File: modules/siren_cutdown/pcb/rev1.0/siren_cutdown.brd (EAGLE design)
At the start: 23.8 x 33.5 mm, 18 parts, among them IC2 PICAXE-08M2

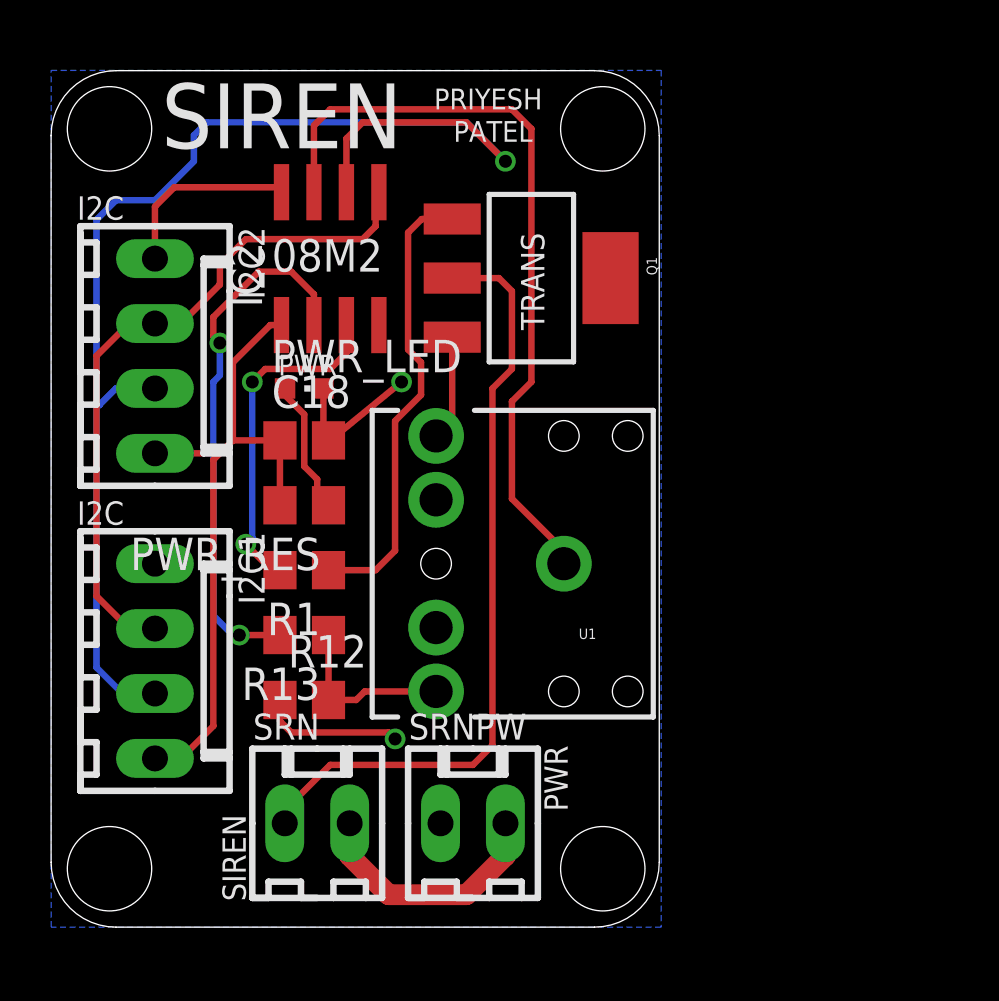
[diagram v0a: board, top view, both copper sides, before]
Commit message: added cutdown to siren
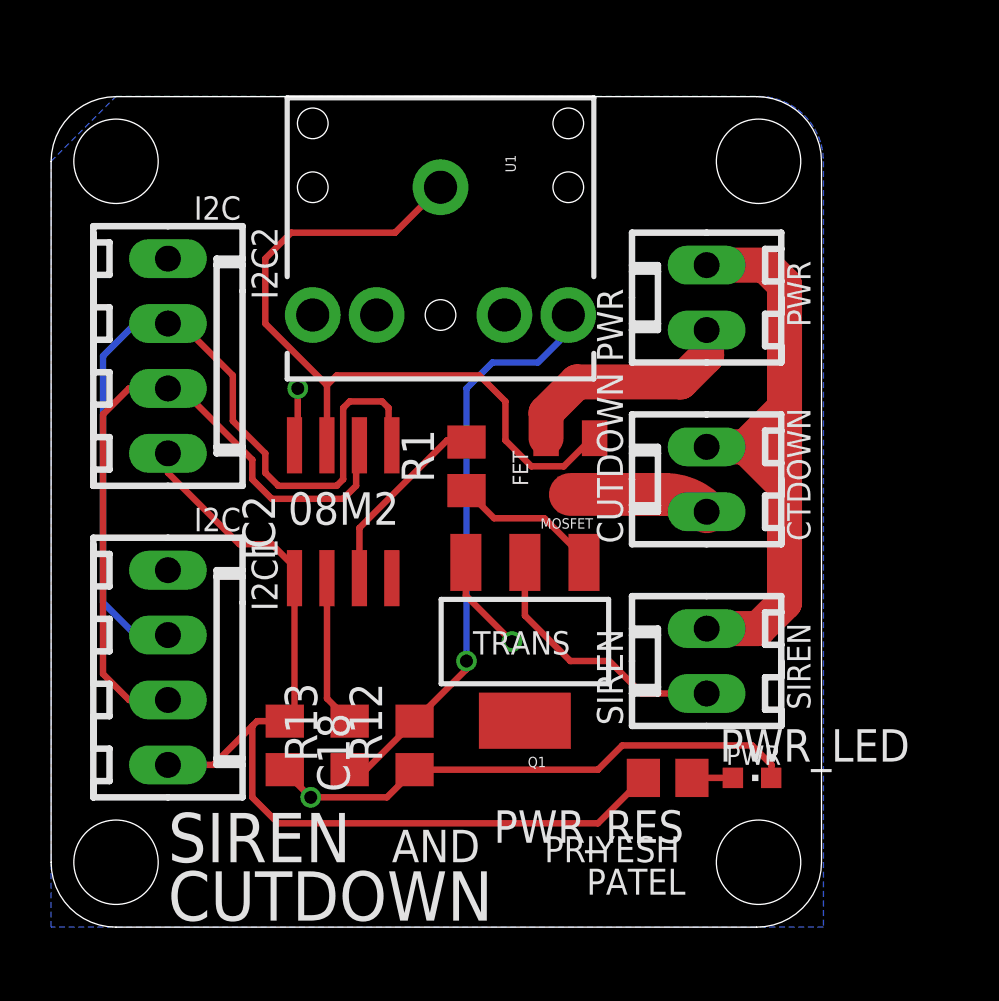
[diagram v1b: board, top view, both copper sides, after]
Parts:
- removed SRN: Siren-Header, apex:6410-02
- removed SRNPW: Siren-Power, apex:6410-02
- added CUTDOWN: Cutdown, apex:6410-02
- added MOSFET: (no value), SparkFun:SOT23
- added PWR: Siren-Power, apex:6410-02
- added SIREN: Siren, apex:6410-02
- moved PWR_LED 23.2 mm to (27.4, 5.84)
- moved PWR_RES 17.8 mm to (24.1, 5.84)
- moved U1 15.5 mm to (15.2, 29.0), turned to 270 degrees
- moved Q1 14.2 mm to (18.5, 11.2), turned to 180 degrees
- moved C18 12.0 mm to (9.14, 7.11), turned to 270 degrees
- moved JP1 10.5 mm to (21.3, 22.1)
- moved IC2 9.92 mm to (11.4, 16.3)
- moved R1 7.54 mm to (16.3, 18.0), turned to 90 degrees
- moved JP3 6.23 mm to (27.7, 30.0)
- moved JP5 6.10 mm to (27.7, 2.54)
- moved R12 4.67 mm to (14.2, 7.11), turned to 90 degrees
- moved R13 4.67 mm to (11.7, 7.11), turned to 90 degrees
- moved JP2 1.30 mm to (2.54, 30.0)
- moved I2C1 0.57 mm to (4.57, 10.2)
- moved I2C2 0.51 mm to (4.57, 22.4)
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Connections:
- removed net N$18: IC2.7, U1.SLEEVE
- new net CUTDOWN: IC2.7, MOSFET.1, U1.SLEEVE
- new net N$4: CUTDOWN.2, MOSFET.3
- net GND: now also MOSFET.2, PWR.2; no longer SRNPW.2
- net N$2: now also SIREN.2; no longer SRN.2
- net VCC: now also CUTDOWN.1, PWR.1, SIREN.1; no longer SRN.1, SRNPW.1
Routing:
- net N$18: track 29.9 -> 0.00 mm
- net CUTDOWN: track 0.00 -> 29.8 mm
- net SCL: track 50.8 -> 27.5 mm, vias 1 -> 0
- net N$2: track 30.3 -> 10.5 mm
- net VCC: track 9.90 -> 26.8 mm
- net N$20: track 6.89 -> 22.8 mm, vias 0 -> 1
- net N$17: track 21.1 -> 5.96 mm, vias 2 -> 0
- net GND: track 22.9 -> 36.5 mm, vias 2 -> 3
- net N$1: track 17.9 -> 5.87 mm
- net 3.3V: track 26.8 -> 38.0 mm
- net SDA: track 27.1 -> 33.2 mm
- net SIREN: track 13.5 -> 7.60 mm, vias 2 -> 0
- net N$4: track 0.00 -> 5.47 mm
- net N$21: track 5.28 -> 1.60 mm
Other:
- board size 23.8 x 33.5 mm -> 30.1 x 32.5 mm
- board text added: "AND"
- board text added: "CTDOWN"
- board text added: "CUTDOWN"
- board text added: "FET"

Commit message: siren pcb
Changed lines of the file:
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@@
 <setting verticaltext="up"/>
 </settings>
-<grid distance="0.01" unitdist="inch" unit="inch" style="lines" multiple="1" display="yes" altdistance="0.005" altunitdist="inch" altunit="inch"/>
+<grid distance="0.05" unitdist="inch" unit="inch" style="lines" multiple="1" display="yes" altdistance="0.005" altunitdist="inch" altunit="inch"/>
 <layers>
 <layer number="1" name="Top" color="4" fill="1" visible="yes" active="yes"/>
@@
 <polygon width="0.254" layer="16" isolate="0.254">
 <vertex x="0" y="0"/>
-<vertex x="0" y="29.972"/>
-<vertex x="2.54" y="32.512"/>
-<vertex x="27.686" y="32.512" curve="-90"/>
-<vertex x="30.226" y="29.972"/>
+<vertex x="0" y="32.512"/>
+<vertex x="30.226" y="32.512"/>
 <vertex x="30.226" y="0"/>
 </polygon>
@@
 <wire x1="27.178" y1="18.796" x2="28.702" y2="20.32" width="1.3716" layer="1"/>
 <wire x1="27.178" y1="18.796" x2="28.702" y2="17.272" width="1.3716" layer="1"/>
-<wire x1="28.702" y1="17.272" x2="27.178" y2="18.796" width="0" layer="19" extent="1-16"/>
 </signal>
 <signal name="CUTDOWN">
